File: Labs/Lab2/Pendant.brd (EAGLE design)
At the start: 78.4 x 78.4 mm, 61 parts

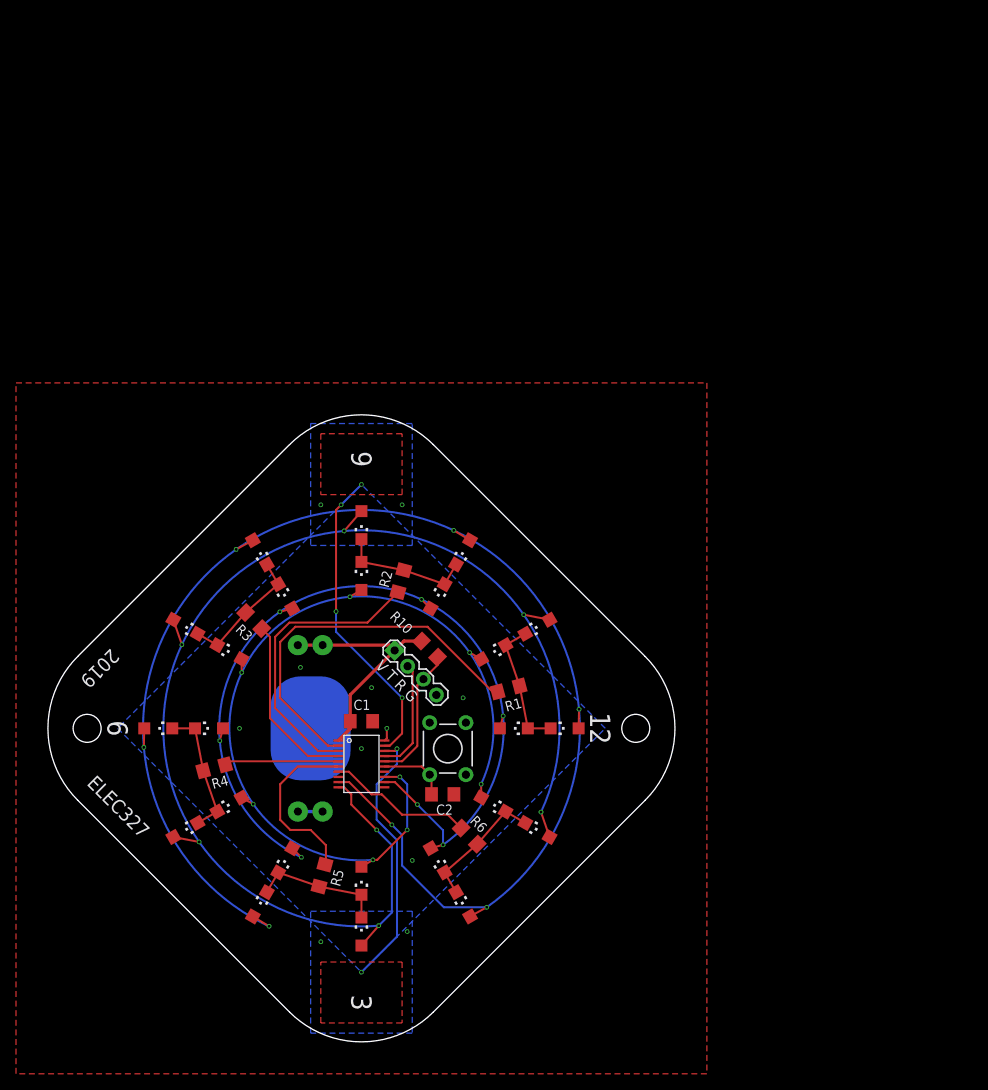
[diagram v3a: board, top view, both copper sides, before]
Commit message: Pendant for 2022 is a 5x7 LED array
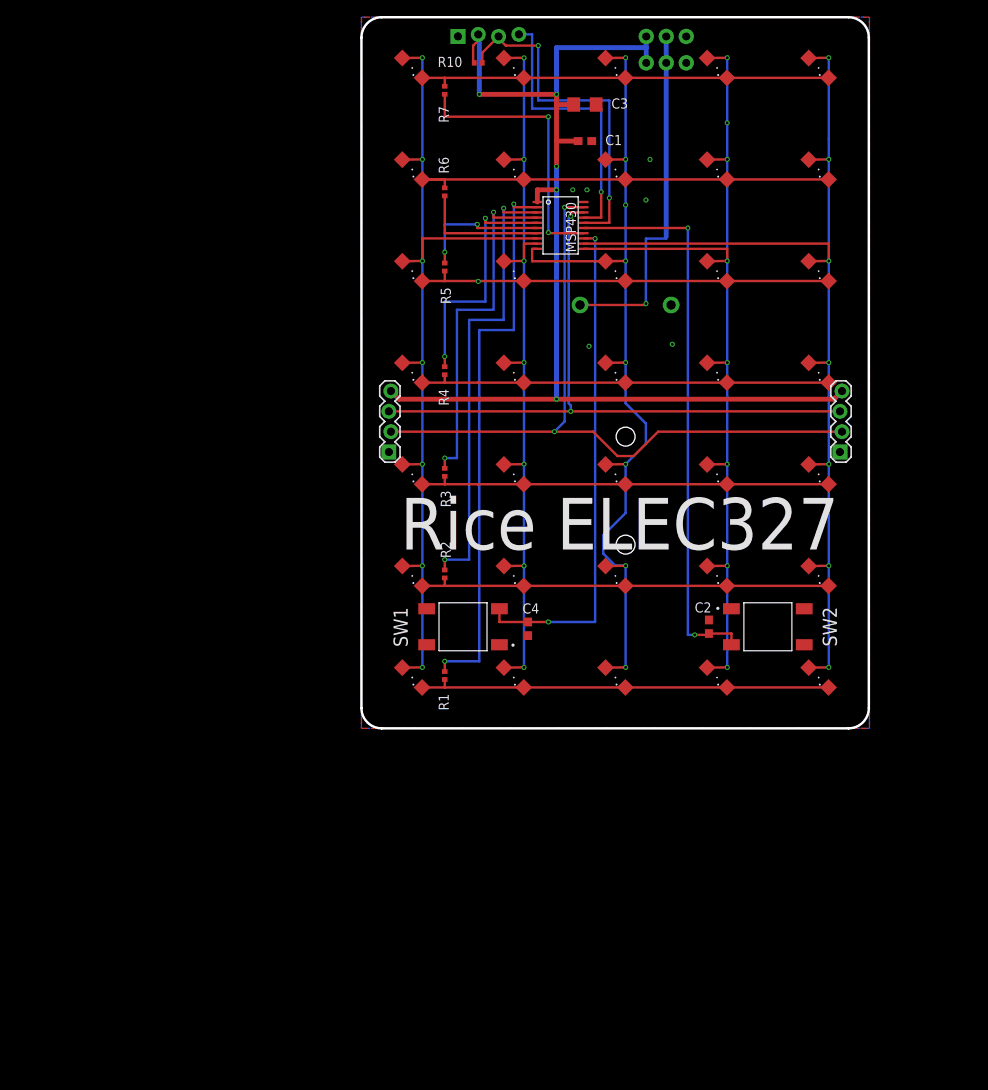
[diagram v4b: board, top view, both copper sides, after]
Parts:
- removed BAT1: 20mm coincell, Battery:BATTCON_20MM_PTH_COMPACT
- removed JP1: (no value), Pendant:1X04_LOCK
- removed LSP1, LSP10, LSP11, LSP12, LSP13, LSP14, LSP15, LSP16, LSP17, LSP18, LSP19, LSP2, LSP20, LSP21, LSP22, LSP23, LSP24, LSP3, LSP4, LSP5, LSP6, LSP7, LSP8, LSP9: LSP10, solpad-mod:LSP10
- removed S1: MOMENTARY-SWITCH-SPST-PTH-6.0MM, SparkFun-Switches:TACTILE_SWITCH_PTH_6.0MM
- added BT1: BC2AAAPC, BC2AAAPC:BAT_BC2AAAPC
- added C3: 100u, rcl:C1206
- added C4: 47nF, rcl:C0603
- added JP2, JP3, TRVG: (no value), Pendant:1X04_LOCK
- added LED25, LED26, LED27, LED28, LED29, LED30, LED31, LED32, LED33, LED34, LED35: (no value), led:SML1206
- added R7: (no value), rcl:R0402
- added SW1, SW2: SWITCH_SPSTSMD, ELEC327:SW_1571563-4
- added U$1: SWITCH_DPDT, ELEC327:JS_DPDT_TH
- C1: value 10u -> 1u; device rcl:C1206 -> rcl:C0603
- C2: value 470nF -> 47nF; device rcl:C1206 -> rcl:C0603
- LED1, LED10, LED11, LED12, LED13, LED14, LED15, LED16, LED17, LED18, LED19, LED2, LED20, LED21, LED22, LED23, LED24, LED3, LED4, LED5, LED6, LED7, LED8, LED9: device led:CHIPLED_1206 -> led:SML1206
- R1, R10, R2, R3, R4, R5, R6: device rcl:R1206 -> rcl:R0402
- moved LED6 92.1 mm to (6.35, 69.8), turned to 135 degrees
- moved LED21 87.5 mm to (31.8, 82.5), turned to 135 degrees
- moved LED5 81.4 mm to (6.35, 57.1), turned to 135 degrees
- moved R6 80.6 mm to (10.4, 67.1), turned to 90 degrees
- moved C1 77.7 mm to (27.9, 73.4)
- moved R5 77.6 mm to (10.4, 57.7), turned to 270 degrees
- moved R10 73.5 mm to (14.6, 83.2), turned to 0 degrees
- moved LED11 72.4 mm to (19.1, 44.5), turned to 135 degrees
- moved MSP430 71.8 mm to (24.9, 62.9)
- moved LED7 71.6 mm to (6.35, 82.5), turned to 135 degrees
- moved LED12 69.9 mm to (19.1, 57.1), turned to 135 degrees
- moved LED13 69.8 mm to (19.1, 69.8), turned to 135 degrees
- moved LED14 66.7 mm to (19.1, 82.5), turned to 135 degrees
- moved LED18 64.9 mm to (31.8, 44.5), turned to 135 degrees
- moved LED17 63.5 mm to (31.8, 31.8), turned to 135 degrees
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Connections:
- removed net CA1: LED1.C, LED13.C, LED19.C, LED7.C, R1.2
- removed net CA2: LED14.C, LED2.C, LED20.C, LED8.C, R2.2
- removed net CA3: LED15.C, LED21.C, LED3.C, LED9.C, R3.2
- removed net CA4: LED10.C, LED16.C, LED22.C, LED4.C, R4.2
- removed net CA5: LED11.C, LED17.C, LED23.C, LED5.C, R5.2
- removed net CA6: LED12.C, LED18.C, LED24.C, LED6.C, R6.2
- removed net CAP1: MSP430.19
- removed net CAP2: MSP430.18
- removed net CB1: LED1.A, LED2.A, LED3.A, LED4.A, LED5.A, LED6.A, LSP1.MP, LSP2.MP, LSP3.MP, LSP4.MP, LSP5.MP, LSP6.MP, MSP430.9
- removed net CB2: LED10.A, LED11.A, LED12.A, LED7.A, LED8.A, LED9.A, LSP10.MP, LSP11.MP, LSP12.MP, LSP7.MP, LSP8.MP, LSP9.MP, MSP430.10
- removed net CB3: LED13.A, LED14.A, LED15.A, LED16.A, LED17.A, LED18.A, LSP13.MP, LSP14.MP, LSP15.MP, LSP16.MP, LSP17.MP, LSP18.MP, MSP430.12
- removed net CB4: LED19.A, LED20.A, LED21.A, LED22.A, LED23.A, LED24.A, LSP19.MP, LSP20.MP, LSP21.MP, LSP22.MP, LSP23.MP, LSP24.MP, MSP430.13
- removed net N$9: MSP430.14
- new net COL1: LED1.A, LED2.A, LED3.A, LED4.A, LED5.A, LED6.A, LED7.A, MSP430.8
- new net COL2: LED10.A, LED11.A, LED12.A, LED13.A, LED14.A, LED8.A, LED9.A, MSP430.9
- new net COL3: LED15.A, LED16.A, LED17.A, LED18.A, LED19.A, LED20.A, LED21.A, MSP430.10
- new net COL4: LED22.A, LED23.A, LED24.A, LED25.A, LED26.A, LED27.A, LED28.A, MSP430.11
- new net COL5: LED29.A, LED30.A, LED31.A, LED32.A, LED33.A, LED34.A, LED35.A, MSP430.12
- new net N$2: BT1.+, U$1.2, U$1.5
- new net ROW1: LED1.C, LED15.C, LED22.C, LED29.C, LED8.C, R1.2
- new net ROW2: LED16.C, LED2.C, LED23.C, LED30.C, LED9.C, R2.2
- new net ROW3: LED10.C, LED17.C, LED24.C, LED3.C, LED31.C, R3.2
- new net ROW4: LED11.C, LED18.C, LED25.C, LED32.C, LED4.C, R4.2
- new net ROW5: LED12.C, LED19.C, LED26.C, LED33.C, LED5.C, R5.2
- new net ROW6: LED13.C, LED20.C, LED27.C, LED34.C, LED6.C, R6.2
- new net ROW7: LED14.C, LED21.C, LED28.C, LED35.C, LED7.C, R7.2
- new net SIG1: JP2.2, JP3.2, MSP430.19
- new net SIG2: JP2.3, JP3.3, MSP430.18
- new net SWITCH2: C2.2, MSP430.15, SW2.3
- net GND: now also BT1.-, C3.2, C4.1, JP2.1, JP3.1, SW1.1, SW2.1, TRVG.1; no longer BAT1.2, JP1.4, S1.3
- net N$1: now also MSP430.14, R7.1; no longer MSP430.8
- net SWITCH1: now also C4.2, MSP430.13, SW1.3; no longer C2.2, MSP430.15, S1.1
- net TEST: now also TRVG.4; no longer JP1.2
- net VDD: now also C3.1, JP2.4, JP3.4, TRVG.2, U$1.1, U$1.4; no longer BAT1.1, BAT1.3, BAT1.4, BAT1.5, JP1.1
- net _RST: now also TRVG.3; no longer JP1.3
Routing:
- net CB1: track 178.1 -> 0.00 mm, vias 1 -> 0
- net CB2: track 164.7 -> 0.00 mm, vias 1 -> 0
- net COL5: track 0.00 -> 126.6 mm, vias 0 -> 7
- net COL4: track 0.00 -> 113.2 mm, vias 0 -> 8
- net VDD: track 33.5 -> 145.5 mm, vias 0 -> 5
- net COL1: track 0.00 -> 110.9 mm, vias 0 -> 7
- net COL3: track 0.00 -> 110.3 mm, vias 0 -> 8
- net CB3: track 110.1 -> 0.00 mm, vias 1 -> 0
- net CB4: track 107.3 -> 0.00 mm, vias 2 -> 0
- net COL2: track 0.00 -> 97.6 mm, vias 0 -> 7
- net SIG1: track 0.00 -> 89.9 mm, vias 0 -> 2
- net SIG2: track 0.00 -> 83.1 mm, vias 0 -> 2
- net SWITCH2: track 0.00 -> 70.9 mm, vias 0 -> 2
- net ROW6: track 0.00 -> 54.7 mm
- net SWITCH1: track 8.61 -> 63.0 mm, vias 0 -> 2
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- removed copper zone on layer 1, net CAP1
- removed copper zone on layer 1, net CAP2
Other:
- board size 78.4 x 78.4 mm -> 63.4 x 88.9 mm
- board text added: "Rice ELEC327"
- board text removed: "12"
- board text removed: "2019"
- board text removed: "3"
- board text removed: "6"
- board text removed: "9"
- board text removed: "ELEC327"
- board text removed: "V T R G"
- board text removed: "sdg"
